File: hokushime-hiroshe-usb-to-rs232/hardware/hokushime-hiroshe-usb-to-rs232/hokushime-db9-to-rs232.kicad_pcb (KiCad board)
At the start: 2 copper layers, 6 parts, among them IC1 SP3243EC/EB, U1 FT232BM/BL, U3 93CxxC

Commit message: [04-22-0550] Hokushime create pcb and basic layout
Update README.md
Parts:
- added C10: 0.1uF, Capacitor_SMD:C_0603_1608Metric_Pad1.08x0.95mm_HandSolder, F.Cu at (128.9, 98.0)
- added C11: 10uF, Capacitor_SMD:C_0603_1608Metric_Pad1.08x0.95mm_HandSolder, F.Cu at (128.9, 96.4)
- added C12: 0.1uF, Capacitor_SMD:C_0603_1608Metric_Pad1.08x0.95mm_HandSolder, F.Cu at (128.9, 94.8)
- added C3: 27pF, Capacitor_SMD:C_0603_1608Metric_Pad1.08x0.95mm_HandSolder, F.Cu at (128.8, 88.7)
- added C4: 0.1uF, Capacitor_SMD:C_0603_1608Metric_Pad1.08x0.95mm_HandSolder, F.Cu at (128.8, 92.3)
- added C5: 33nF, Capacitor_SMD:C_0603_1608Metric_Pad1.08x0.95mm_HandSolder, F.Cu at (128.8, 90.7)
- added C6: 0.22uF/16V, Capacitor_SMD:C_0603_1608Metric_Pad1.08x0.95mm_HandSolder, B.Cu at (150.4, 90.0)
- added C7: 0.22uF/16V, Capacitor_SMD:C_0603_1608Metric_Pad1.08x0.95mm_HandSolder, B.Cu at (143.2, 89.8)
- added C8: 0.22uF/16V, Capacitor_SMD:C_0603_1608Metric_Pad1.08x0.95mm_HandSolder, B.Cu at (147.3, 90.0)
- added C9: 0.22uF/16V, Capacitor_SMD:C_0603_1608Metric_Pad1.08x0.95mm_HandSolder, B.Cu at (145.5, 90.0)
- added D1: TX, LED_SMD:LED_0805_2012Metric_Pad1.15x1.40mm_HandSolder, F.Cu at (125.2, 87.3)
- added D2: RX, LED_SMD:LED_0805_2012Metric_Pad1.15x1.40mm_HandSolder, F.Cu at (125.2, 89.4)
- added FB1: 40 Ohms @100 MHz, Inductor_SMD:L_0603_1608Metric_Pad1.05x0.95mm_HandSolder, F.Cu at (121.0, 95.2)
- added G1: LOGO, external-lib:Crumbs-Logo_Footprint_13x13, B.Cu at (137.9, 94.0)
- added J1: Conn1, Connector_PinHeader_2.54mm:PinHeader_1x07_P2.54mm_Horizontal, F.Cu at (158.2, 95.8)
- added J2: USB_B, Connector_USB:USB_B_Lumberg_2411_02_Horizontal, F.Cu at (117.2, 91.5)
- added J3: Conn2, Connector_PinHeader_2.54mm:PinHeader_1x10_P2.54mm_Horizontal, F.Cu at (135.3, 84.2)
- added JP1: 5V-1, Test-2, GND-3, Jumper:SolderJumper-3_P2.0mm_Open_TrianglePad1.0x1.5mm_NumberLabels, B.Cu at (123.2, 95.0)
- added JP2: CONN2_TO_GND, Jumper:SolderJumper-2_P1.3mm_Open_RoundedPad1.0x1.5mm, B.Cu at (121.5, 98.2)
- added JP3: CONN1_SHIELD_TO_GND, Jumper:SolderJumper-2_P1.3mm_Open_RoundedPad1.0x1.5mm, B.Cu at (124.0, 98.2)
- added R2: 2K2, Resistor_SMD:R_0805_2012Metric_Pad1.20x1.40mm_HandSolder, B.Cu at (156.0, 90.0)
- added R3: 27, Resistor_SMD:R_0805_2012Metric_Pad1.20x1.40mm_HandSolder, F.Cu at (121.2, 91.3)
- added R4: 27, Resistor_SMD:R_0805_2012Metric_Pad1.20x1.40mm_HandSolder, F.Cu at (121.2, 93.3)
- added R5: 470, Resistor_SMD:R_0805_2012Metric_Pad1.20x1.40mm_HandSolder, F.Cu at (125.2, 93.3)
- added R6: 1K5, Resistor_SMD:R_0805_2012Metric_Pad1.20x1.40mm_HandSolder, F.Cu at (125.2, 91.3)
- added R7: 220, Resistor_SMD:R_0805_2012Metric_Pad1.20x1.40mm_HandSolder, F.Cu at (121.2, 87.4)
- added R8: 220, Resistor_SMD:R_0805_2012Metric_Pad1.20x1.40mm_HandSolder, F.Cu at (121.2, 89.4)
- added TP1: Status, TestPoint:TestPoint_Pad_D1.0mm, F.Cu at (142.3, 92.8)
- added Y1: 6Mhz, Crystal:Crystal_HC49-U_Vertical, F.Cu at (122.7, 83.2)
- C1: value C -> 27pF
- C2: value C_Polarized -> 0.22uF/16V; moved to B.Cu
- R1: value R_US -> 10K; moved to B.Cu
- moved R1 73.9 mm to (158.6, 90.0), turned to -90 degrees
- moved C2 67.2 mm to (152.1, 90.0), turned to 90 degrees
- moved U3 65.9 mm to (156.8, 90.0), turned to 90 degrees
- moved IC1 57.2 mm to (148.6, 90.0), turned to 90 degrees
- moved C1 44.3 mm to (128.8, 87.2)
- moved U1 33.5 mm to (135.9, 91.5), turned to 90 degrees
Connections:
- C1 pad 1: unconnected-(C1-Pad1) -> Net-(U1-XTIN)
- C1 pad 2: unconnected-(C1-Pad2) -> GND
- C2 pad 1: unconnected-(C2-Pad1) -> Net-(IC1-C1+)
- C2 pad 2: unconnected-(C2-Pad2) -> Net-(IC1-C1-)
- IC1 pad 1: unconnected-(IC1-C2+-Pad1) -> Net-(IC1-C2+)
- IC1 pad 10: unconnected-(IC1-T2OUT-Pad10) -> /CONN2_RTS
- IC1 pad 11: unconnected-(IC1-T3OUT-Pad11) -> /CONN2_DTR
- IC1 pad 12: unconnected-(IC1-T3IN-Pad12) -> /~{DTR}
- IC1 pad 13: unconnected-(IC1-T2IN-Pad13) -> /~{RTS}
- IC1 pad 14: unconnected-(IC1-T1IN-Pad14) -> /TXD
- IC1 pad 15: unconnected-(IC1-R5OUT-Pad15) -> /~{RI}
- IC1 pad 16: unconnected-(IC1-R4OUT-Pad16) -> /~{DCD}
- IC1 pad 17: unconnected-(IC1-R3OUT-Pad17) -> /~{DSR}
- IC1 pad 18: unconnected-(IC1-R2OUT-Pad18) -> /~{CTS}
- IC1 pad 19: unconnected-(IC1-R1OUT-Pad19) -> /RXD
- IC1 pad 2: unconnected-(IC1-C2--Pad2) -> Net-(IC1-C2-)
- IC1 pad 21: unconnected-(IC1-~{STATUS}-Pad21) -> Net-(IC1-~{STATUS})
- IC1 pad 22: unconnected-(IC1-~{SHUTDOWN}-Pad22) -> /~{SLEEP}
- IC1 pad 23: unconnected-(IC1-~{ONLINE}-Pad23) -> GND
- IC1 pad 24: unconnected-(IC1-C1--Pad24) -> Net-(IC1-C1-)
- IC1 pad 25: unconnected-(IC1-GND-Pad25) -> GND
- IC1 pad 26: unconnected-(IC1-VCC-Pad26) -> +5V
- IC1 pad 27: unconnected-(IC1-V+-Pad27) -> Net-(IC1-V+)
- IC1 pad 28: unconnected-(IC1-C1+-Pad28) -> Net-(IC1-C1+)
- IC1 pad 3: unconnected-(IC1-V--Pad3) -> Net-(IC1-V-)
- IC1 pad 4: unconnected-(IC1-R1IN-Pad4) -> /CONN2_RXD
- IC1 pad 5: unconnected-(IC1-R2IN-Pad5) -> /CONN2_CTS
- IC1 pad 6: unconnected-(IC1-R3IN-Pad6) -> /CONN2_DSR
- IC1 pad 7: unconnected-(IC1-R4IN-Pad7) -> /CONN2_DCD
- IC1 pad 8: unconnected-(IC1-R5IN-Pad8) -> /CONN2_RI
- IC1 pad 9: unconnected-(IC1-T1OUT-Pad9) -> /CONN2_TXD
- R1 pad 1: unconnected-(R1-Pad1) -> +5V
- R1 pad 2: unconnected-(R1-Pad2) -> /93C66_DO
- U1 pad 1: unconnected-(U1-EESK-Pad1) -> /93C66_SCLK
- U1 pad 10: unconnected-(U1-~{SLEEP}-Pad10) -> /~{SLEEP}
- U1 pad 11: unconnected-(U1-~{RXLED}-Pad11) -> Net-(U1-~{RXLED})
- U1 pad 12: unconnected-(U1-~{TXLED}-Pad12) -> Net-(U1-~{TXLED})
- U1 pad 13: unconnected-(U1-VCCIO-Pad13) -> +5V
- U1 pad 14: unconnected-(U1-PWRCTL-Pad14) -> GND
- U1 pad 17: unconnected-(U1-GND-Pad17) -> GND
- U1 pad 18: unconnected-(U1-D7/~{RI}-Pad18) -> /~{RI}
- U1 pad 19: unconnected-(U1-D6/~{DCD}-Pad19) -> /~{DCD}
- U1 pad 2: unconnected-(U1-EEDATA-Pad2) -> /93C66_DI
- U1 pad 20: unconnected-(U1-D5/~{DSR}-Pad20) -> /~{DSR}
- U1 pad 21: unconnected-(U1-D4/~{DTR}-Pad21) -> /~{DTR}
- U1 pad 22: unconnected-(U1-D3/~{CTS}-Pad22) -> /~{CTS}
- U1 pad 23: unconnected-(U1-D2/~{RST}-Pad23) -> /~{RTS}
- U1 pad 24: unconnected-(U1-D1/RXD-Pad24) -> /RXD
- U1 pad 25: unconnected-(U1-D0/TXD-Pad25) -> /TXD
- U1 pad 26: unconnected-(U1-VCC-Pad26) -> +5V
- U1 pad 27: unconnected-(U1-XTIN-Pad27) -> Net-(U1-XTIN)
- U1 pad 28: unconnected-(U1-XTOUT-Pad28) -> Net-(U1-XTOUT)
- U1 pad 29: unconnected-(U1-AGND-Pad29) -> GND
- U1 pad 3: unconnected-(U1-VCC-Pad3) -> +5V
- U1 pad 30: unconnected-(U1-AVCC-Pad30) -> Net-(U1-AVCC)
- U1 pad 31: unconnected-(U1-TEST-Pad31) -> Net-(JP1-C)
- U1 pad 32: unconnected-(U1-EECS-Pad32) -> /93C66_CS
- U1 pad 4: unconnected-(U1-~{RESET}-Pad4) -> +5V
- U1 pad 5: unconnected-(U1-~{RSTOUT}-Pad5) -> Net-(U1-~{RSTOUT})
- U1 pad 6: unconnected-(U1-3V3OUT-Pad6) -> Net-(U1-3V3OUT)
- U1 pad 7: unconnected-(U1-USBDP-Pad7) -> Net-(U1-USBDP)
- U1 pad 8: unconnected-(U1-USBDM-Pad8) -> Net-(U1-USBDM)
- U1 pad 9: unconnected-(U1-GND-Pad9) -> GND
- U3 pad 1: unconnected-(U3-CS-Pad1) -> /93C66_CS
- U3 pad 2: unconnected-(U3-SCLK-Pad2) -> /93C66_SCLK
- U3 pad 3: unconnected-(U3-DI-Pad3) -> /93C66_DI
- U3 pad 4: unconnected-(U3-DO-Pad4) -> /93C66_DO
- U3 pad 5: unconnected-(U3-GND-Pad5) -> GND
- U3 pad 6: unconnected-(U3-ORG-Pad6) -> +5V
- U3 pad 8: unconnected-(U3-VCC-Pad8) -> +5V
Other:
- board outline added: 51.5 x 20.1 mm
- board text added: "HOKUSHIME"

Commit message: [04-22-1840] thing about vias making
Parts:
- C10, C11, C12, R3, R4, TP1, Y1: moved to B.Cu
- moved JP2 33.1 mm to (144.9, 74.8), turned to 180 degrees
- moved R2 21.8 mm to (134.2, 90.3)
- moved TP1 20.5 mm to (152.3, 74.9)
- moved JP3 20.3 mm to (143.4, 104.2), turned to 180 degrees
- moved R1 19.3 mm to (139.3, 90.3)
- moved U3 18.9 mm to (137.9, 90.3)
- moved R8 17.9 mm to (137.6, 96.7), turned to 90 degrees
- moved R5 16.6 mm to (126.2, 76.7)
- moved C7 15.8 mm to (159.0, 89.8)
- moved C4 15.3 mm to (122.2, 78.5)
- moved R7 13.6 mm to (131.2, 96.7), turned to 90 degrees
- moved D2 12.6 mm to (135.4, 96.7), turned to 90 degrees
- moved D1 12.4 mm to (133.2, 96.7), turned to 90 degrees
- moved C3 12.4 mm to (131.3, 76.5), turned to 0 degrees
- moved C12 12.3 mm to (116.6, 94.3)
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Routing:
- net GND: track 0.00 -> 55.2 mm, vias 0 -> 1
- net +5V: track 0.00 -> 32.3 mm, vias 0 -> 2
- net Net-(U1-~{RXLED}): track 0.00 -> 16.2 mm
- net Net-(JP1-C): track 0.00 -> 9.80 mm, vias 0 -> 1
- net Net-(U1-3V3OUT): track 0.00 -> 6.44 mm
- net /USBD+: track 0.00 -> 5.47 mm
- net Net-(U1-XTIN): track 0.00 -> 4.36 mm
- net Net-(U1-XTOUT): track 0.00 -> 3.41 mm
- net VBUS: track 0.00 -> 3.08 mm
- net /CONN2_RI: track 0.00 -> 2.94 mm
- net /CONN2_RTS: track 0.00 -> 2.82 mm
- net /CONN2_TXD: track 0.00 -> 2.79 mm
- net /CONN2_DTR: track 0.00 -> 2.73 mm
- net /~{DTR}: track 0.00 -> 2.72 mm
- net /USBD-: track 0.00 -> 2.71 mm
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
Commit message: [04-24-1904] pcb routing finished
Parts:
- added G1: LOGO, external-lib:Crumbs-Logo_Footprint_13x13, F.Cu at (174.9, 101.2)
- added H1: MountingHole, MountingHole:MountingHole_3mm, F.Cu at (150.3, 76.2)
- added H2: MountingHole, MountingHole:MountingHole_3mm, F.Cu at (130.2, 97.5)
- added H4: MountingHole, MountingHole:MountingHole_3mm, F.Cu at (175.9, 117.0)
- C10, C11, C12, C2, C6, C7, C8, C9, JP1, JP2, JP3, R1, R2, R3, R4, TP1, Y1: moved to F.Cu
- moved C12 38.4 mm to (153.4, 105.2)
- moved C11 37.6 mm to (153.4, 103.7)
- moved C10 37.1 mm to (153.4, 102.1)
- moved G1 35.8 mm to (166.3, 115.8)
- moved JP2 34.0 mm to (172.4, 94.9)
- moved FB1 31.5 mm to (148.7, 105.3), turned to 0 degrees
- moved R4 28.0 mm to (141.0, 99.8), turned to 0 degrees
- moved R3 26.0 mm to (141.0, 97.7), turned to 0 degrees
- moved TP1 26.0 mm to (160.1, 99.7)
- moved C6 25.6 mm to (168.0, 97.8), turned to 90 degrees
- moved C2 25.2 mm to (163.7, 102.4), turned to 180 degrees
- moved J2 24.5 mm to (138.5, 103.5), turned to -90 degrees
- moved JP1 20.7 mm to (133.6, 77.9)
- moved J3 20.7 mm to (154.7, 87.5)
- moved C1 20.6 mm to (151.6, 81.5), turned to 90 degrees
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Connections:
- J3 pad 2: /CONN2_TXD -> /CONN2_RTS
- J3 pad 3: /CONN2_RXD -> /CONN2_TXD
- J3 pad 4: /CONN2_DSR -> /CONN2_RI
- J3 pad 5: /CONN2_GND -> /CONN2_DCD
- J3 pad 6: /CONN2_DCD -> /CONN2_DSR
- J3 pad 8: /CONN2_RTS -> /CONN2_RXD
- J3 pad 9: /CONN2_RI -> /CONN2_GND
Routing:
- net GND: track 55.2 -> 210.9 mm, vias 1 -> 16
- net +5V: track 32.3 -> 178.1 mm, vias 2 -> 4
- net /USBD+: track 5.47 -> 71.8 mm, vias 0 -> 2
- net /USBD-: track 2.71 -> 51.8 mm
- net VBUS: track 3.08 -> 47.4 mm, vias 0 -> 2
- net /93C66_CS: track 0.00 -> 38.2 mm
- net /~{SLEEP}: track 2.48 -> 27.7 mm, vias 0 -> 2
- net Net-(U1-AVCC): track 0.00 -> 23.2 mm
- net Net-(U1-XTOUT): track 3.41 -> 17.1 mm
- net /RXD: track 2.34 -> 15.7 mm, vias 0 -> 2
- net /93C66_DI: track 0.00 -> 13.3 mm
- net Net-(U1-USBDP): track 2.69 -> 14.3 mm
- net Net-(JP1-C): track 9.80 -> 21.1 mm, vias 1 -> 2
- net /~{CTS}: track 2.11 -> 12.6 mm, vias 0 -> 2
- net /~{DSR}: track 1.81 -> 12.1 mm
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- added copper zone on F.Cu, net +5V
- added copper zone on B.Cu, net GND
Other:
- board size 51.5 x 20.1 mm -> 52.4 x 47.7 mm
- board text added: "2025 APRIL 24"
- board text added: "Assembled with Love and a soldering iron Powered by electrons and good vibes 01010011 01101111 01101100 01100100 01100101 01110010 00100001 Debug me if you can Built with coffe and late-night commits This PCB contains 0% AI. 100% sweat. Code, solder, coffee, repeat Beep Boop Circuit Activated Open source. Open heart. Closed loops. This board was debugged with mild panic"

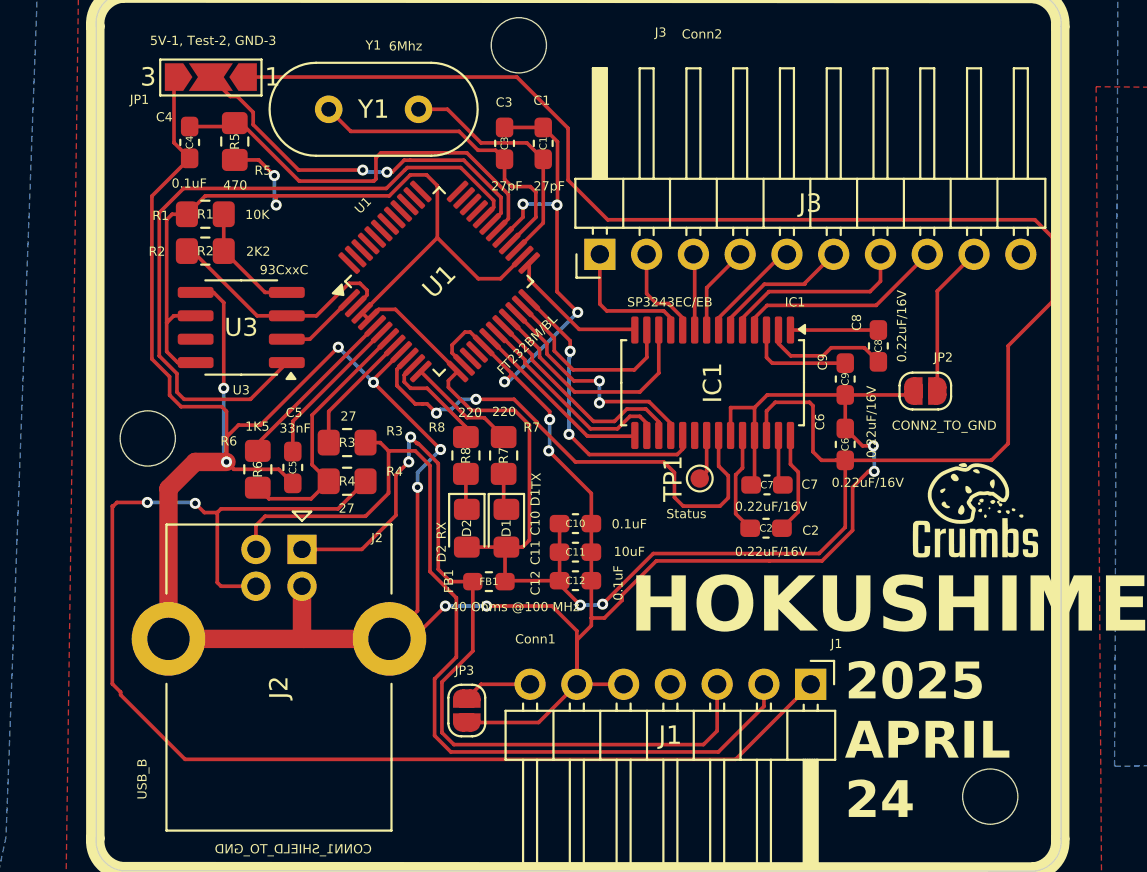
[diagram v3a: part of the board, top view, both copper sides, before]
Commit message: [05-16-1248] change vias to 0.8 mm for manual driling
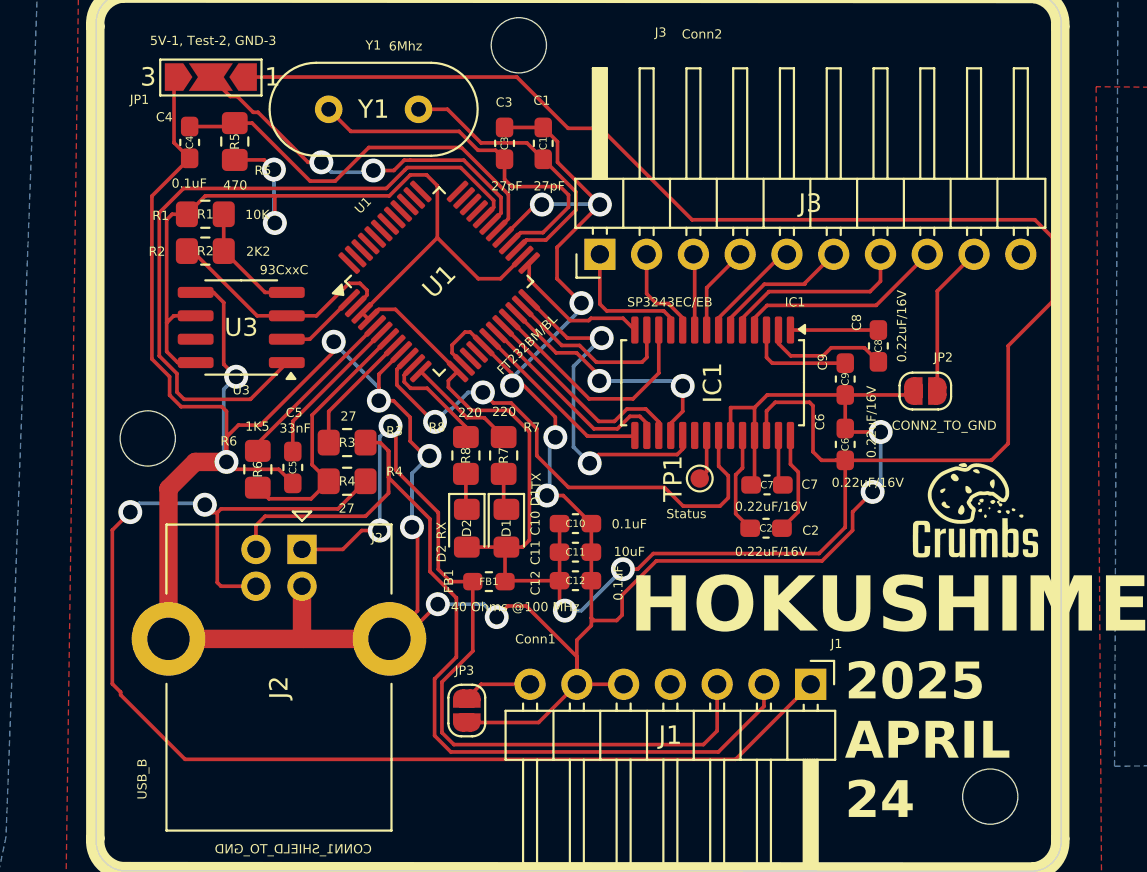
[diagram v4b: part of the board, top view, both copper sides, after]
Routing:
- net GND: track 210.9 -> 219.2 mm
- net Net-(U1-XTOUT): track 17.1 -> 20.3 mm
- net /RXD: track 15.7 -> 18.7 mm
- net Net-(U1-XTIN): track 13.4 -> 15.5 mm
- net /~{CTS}: track 12.6 -> 13.8 mm
- net VBUS: track 47.4 -> 48.6 mm
- net +5V: track 178.1 -> 179.2 mm
- net /USBD-: track 51.8 -> 50.9 mm
- net /USBD+: track 71.8 -> 71.0 mm
- net /~{RTS}: track 10.3 -> 9.59 mm
- net /~{SLEEP}: track 27.7 -> 28.4 mm

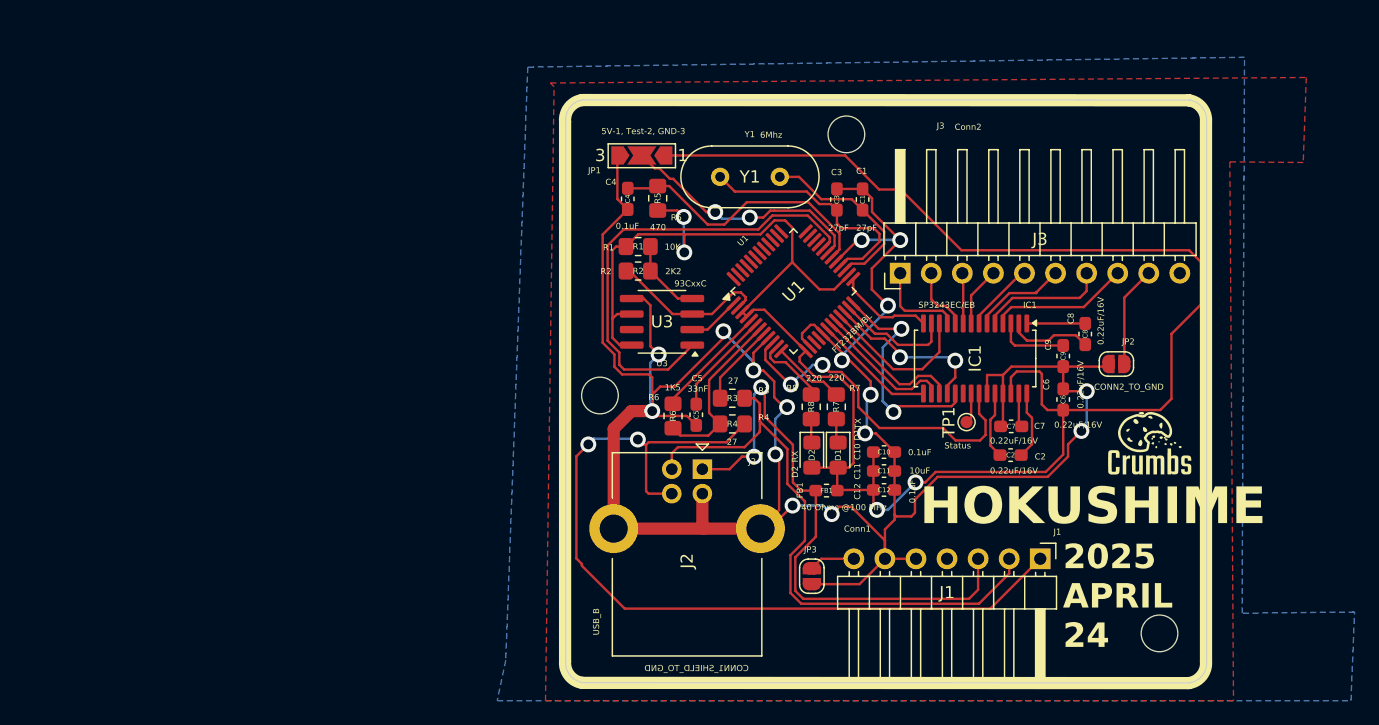
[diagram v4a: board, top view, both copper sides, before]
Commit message: [05-18-0917] re-routing and flip component
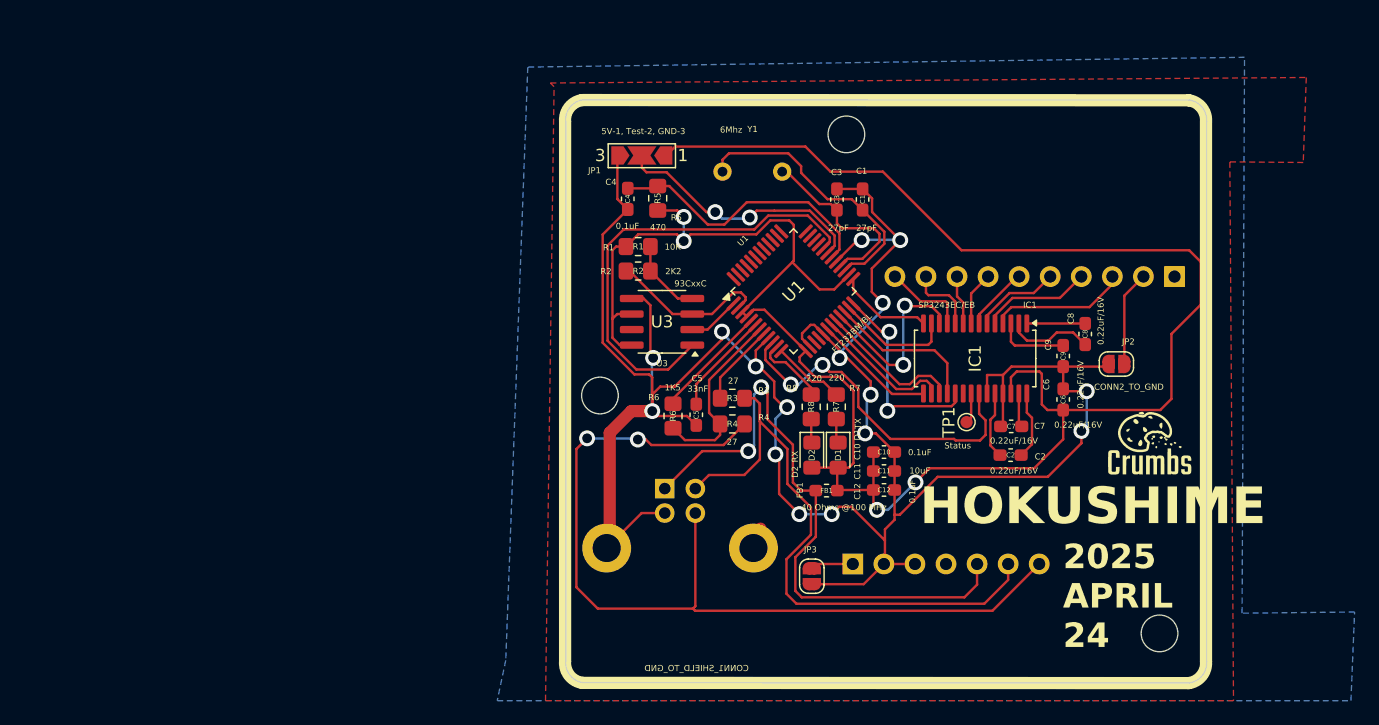
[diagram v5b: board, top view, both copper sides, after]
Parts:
- J1, J2, J3, Y1: moved to B.Cu
- moved J3 22.4 mm to (177.1, 87.8)
- moved G1 18.9 mm to (162.5, 97.2)
- moved J1 15.3 mm to (150.8, 111.3)
- moved Y1 5.09 mm to (145.1, 79.2), turned to 180 degrees
- moved J2 3.46 mm to (135.4, 105.1)
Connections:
- J1 pad 1: /USBD+ -> Net-(J1-Pin_1)
- J1 pad 2: /USBD- -> GND
- J1 pad 3: VBUS -> GND
- J1 pad 5: GND -> VBUS
- J1 pad 6: GND -> /USBD-
- J1 pad 7: Net-(J1-Pin_7) -> /USBD+
- J3 pad 1: /CONN2_DTR -> /CONN2_SHIELD
- J3 pad 10: /CONN2_SHIELD -> /CONN2_DTR
- J3 pad 2: /CONN2_RTS -> /CONN2_GND
- J3 pad 3: /CONN2_TXD -> /CONN2_RXD
- J3 pad 4: /CONN2_RI -> /CONN2_CTS
- J3 pad 5: /CONN2_DCD -> /CONN2_DSR
- J3 pad 6: /CONN2_DSR -> /CONN2_DCD
- J3 pad 7: /CONN2_CTS -> /CONN2_RI
- J3 pad 8: /CONN2_RXD -> /CONN2_TXD
- J3 pad 9: /CONN2_GND -> /CONN2_RTS
- JP3 pad 2: Net-(J1-Pin_7) -> Net-(J1-Pin_1)
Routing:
- net GND: track 219.2 -> 201.8 mm
- net Net-(U1-XTIN): track 15.5 -> 22.5 mm
- net Net-(U1-XTOUT): track 20.3 -> 15.4 mm
- net Net-(J1-Pin_7): track 3.76 -> 0.00 mm
- net Net-(J1-Pin_1): track 0.00 -> 3.58 mm
- net /USBD+: track 71.0 -> 74.5 mm
- net /~{DTR}: track 12.8 -> 15.6 mm, vias 0 -> 2
- net VBUS: track 48.6 -> 50.9 mm
- net +5V: track 179.2 -> 177.4 mm
- net /RXD: track 18.7 -> 17.0 mm
- net /CONN2_CTS: track 10.4 -> 9.03 mm
- net Net-(U1-USBDP): track 14.3 -> 15.1 mm
- net /CONN2_DTR: track 7.52 -> 6.85 mm
- net /93C66_CS: track 38.2 -> 37.6 mm
- net Net-(JP1-C): track 20.7 -> 21.3 mm
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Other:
- board text added: "CONN1_GND"
- board text added: "CONN1_GND_"
- board text added: "CONN1_USBD+"
- board text added: "CONN1_USBD-"
- board text added: "CONN1_VBUS"
- board text added: "CONN2_CTS"
- board text added: "CONN2_DCD"
- board text added: "CONN2_DSR"
- board text added: "CONN2_DTR"
- board text added: "CONN2_GND"
- board text added: "CONN2_RI"
- board text added: "CONN2_RTS"
- board text added: "CONN2_RXD"
- board text added: "CONN2_SHD"
- board text added: "CONN2_TXD"
- board text removed: "Assembled with Love and a soldering iron Powered by electrons and good vibes 01010011 01101111 01101100 01100100 01100101 01110010 00100001 Debug me if you can Built with coffe and late-night commits This PCB contains 0% AI. 100% sweat. Code, solder, coffee, repeat Beep Boop Circuit Activated Open source. Open heart. Closed loops. This board was debugged with mild panic"

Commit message: [05-18-1145] make manufacturing file, look good, but drill is missing, need to buy one
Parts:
- moved G1 12.9 mm to (175.2, 99.4)
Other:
- board text added: "Connect this Solder Connector to Connect Conn1 SHIELD to PCB GND"
- board text added: "Connect this Solder Connector to Connect Conn2 gnd to PCB GND"
- board text added: "Connect this to GND to make FT232 run at NORMAL mode"
